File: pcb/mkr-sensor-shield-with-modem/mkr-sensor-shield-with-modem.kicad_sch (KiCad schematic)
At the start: 32 parts, among them J1 Conn_01x03_Pin, J10 Conn_01x03_Pin, J11 Conn_01x03_Pin, J12 Conn_01x03_Pin, J13 Conn_01x03_Pin, J14 Conn_01x03_Pin, J15 Conn_01x03_Pin, J16 Conn_01x03_Pin, J17 Conn_01x03_Pin, J18 Conn_01x03_Pin, J19 Conn_02x06_Odd_Even, J2 Conn_01x03_Pin, J20 Conn_02x03_Odd_Even, J21 Conn_01x02_Pin, J23 Conn_01x02_Pin, J3 Conn_01x03_Pin, J4 Conn_01x03_Pin, J5 Conn_01x03_Pin, J6 Conn_01x03_Pin, J7 Conn_01x03_Pin, J8 Conn_01x03_Pin, J9 Conn_01x03_Pin, SW1 SW_Push, U1 L7805

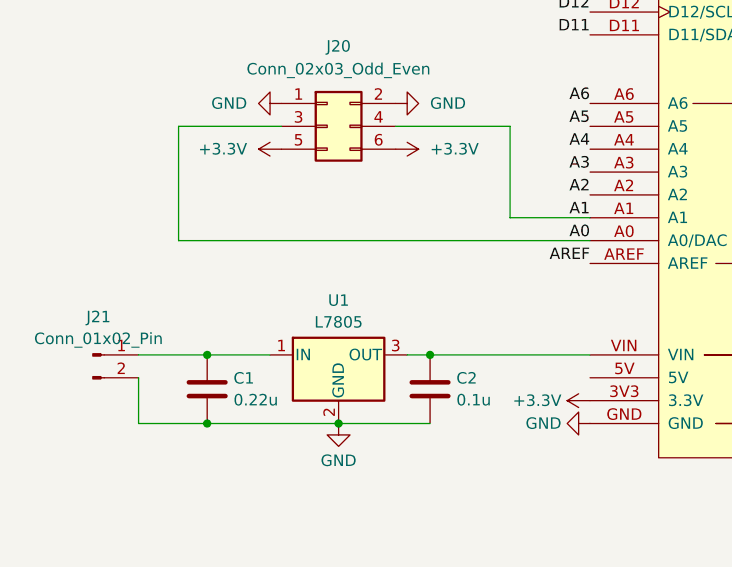
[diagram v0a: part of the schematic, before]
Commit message: Remove backups from repo.  Add jumper to bypass voltage regulator
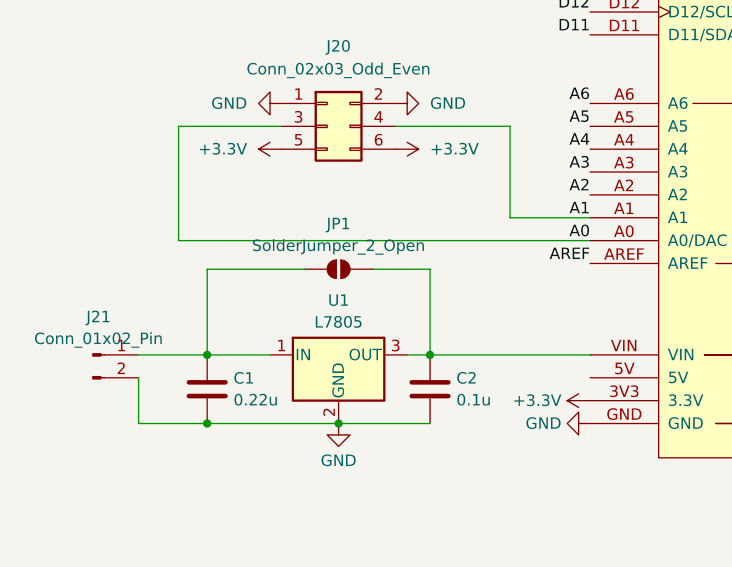
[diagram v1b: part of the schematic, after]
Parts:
- added JP1: SolderJumper_2_Open, Jumper:SolderJumper-2_P1.3mm_Open_TrianglePad1.0x1.5mm, symbol Jumper:SolderJumper_2_Open
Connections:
- net at C1.1, J21.1 (Pin_1), U1.1 (IN): now also JP1.1 (A)
- net at A1.VIN, C2.1, U1.3 (OUT): now also JP1.2 (B)
